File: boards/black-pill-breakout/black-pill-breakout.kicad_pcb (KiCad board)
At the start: 2 copper layers, 79 x 47 mm, 24 parts

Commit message: Layout idea #2
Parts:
- removed the REF** at (124.5, 78.7)
- removed the REF** at (144.8, 81.3)
- removed the REF** at (144.8, 83.8)
- removed the REF** at (182.9, 96.5)
- removed the REF** at (200.7, 87.6)
- removed the REF** at (124.5, 81.3)
- removed the REF** at (200.7, 90.2)
- removed the REF** at (144.8, 78.7)
- removed the REF** at (200.7, 85.1)
- removed the REF** at (124.5, 83.8)
- added REF**: PinSocket_1x06_P2.54mm_Vertical, Connector_PinSocket_2.54mm:PinSocket_1x06_P2.54mm_Vertical, F.Cu at (147.3, 83.8)
- added REF**: PinSocket_1x06_P2.54mm_Vertical, Connector_PinSocket_2.54mm:PinSocket_1x06_P2.54mm_Vertical, F.Cu at (167.6, 83.8)
- added REF**: PinSocket_1x06_P2.54mm_Vertical, Connector_PinSocket_2.54mm:PinSocket_1x06_P2.54mm_Vertical, F.Cu at (147.3, 81.3)
- added REF**: PinSocket_1x06_P2.54mm_Vertical, Connector_PinSocket_2.54mm:PinSocket_1x06_P2.54mm_Vertical, F.Cu at (167.6, 78.7)
- added REF**: PinSocket_1x06_P2.54mm_Vertical, Connector_PinSocket_2.54mm:PinSocket_1x06_P2.54mm_Vertical, F.Cu at (147.3, 78.7)
- added REF**: PinSocket_1x06_P2.54mm_Vertical, Connector_PinSocket_2.54mm:PinSocket_1x06_P2.54mm_Vertical, F.Cu at (167.6, 81.3)
- moved REF** 42.1 mm to (137.2, 81.3), turned to 270 degrees
- moved REF** 5.39 mm to (181.6, 97.8)
- moved REF** 4.43 mm to (148.6, 104.1)

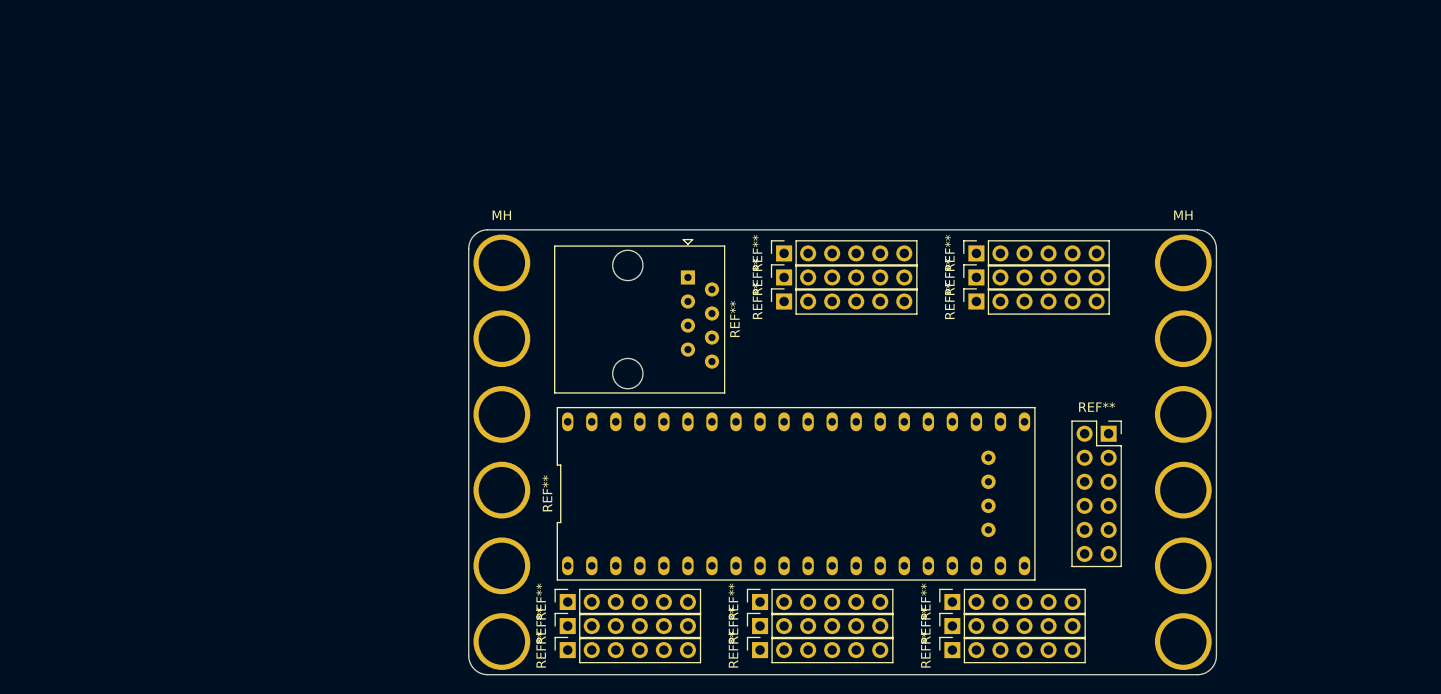
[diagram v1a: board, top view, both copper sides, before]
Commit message: Done routing, pre-silkscreen
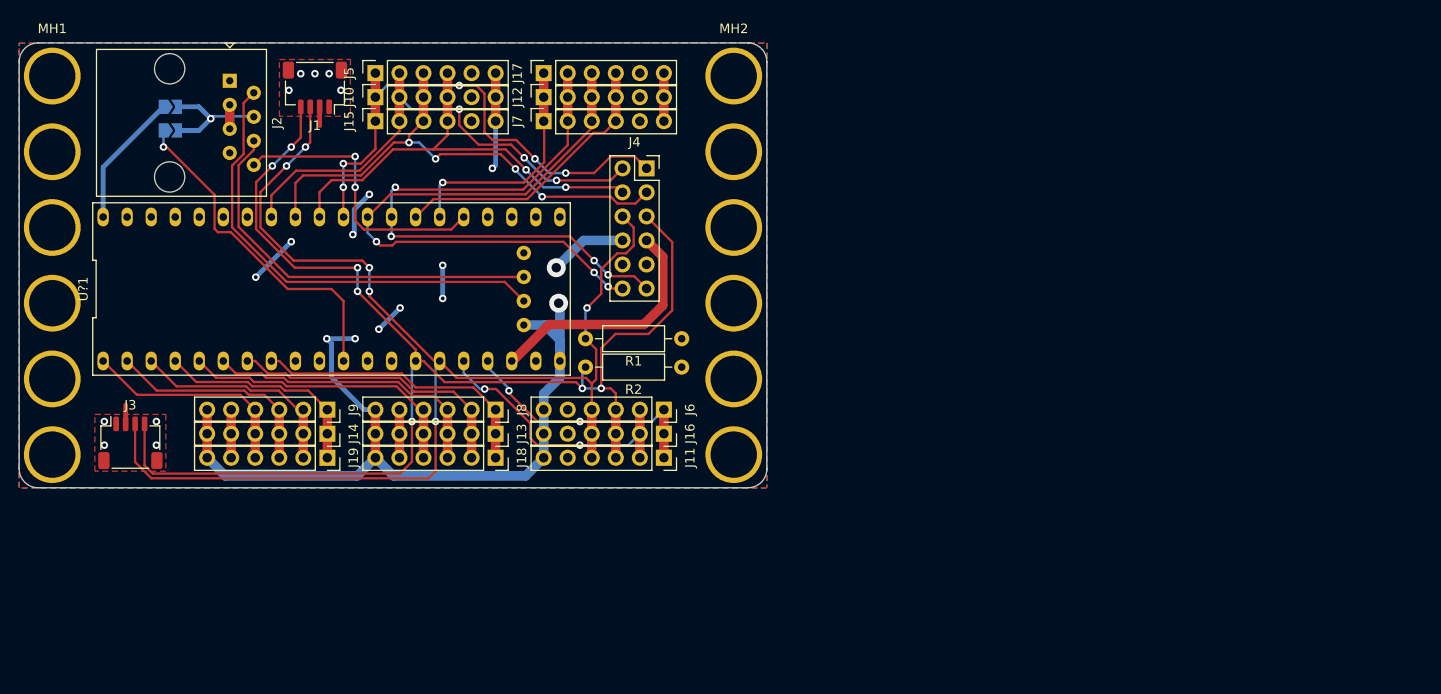
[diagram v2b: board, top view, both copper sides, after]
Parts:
- removed MH (x2): brick-1x6, brick-4_9id-6_0od:brick-1x6
- removed REF** (x15): PinSocket_1x06_P2.54mm_Vertical, Connector_PinSocket_2.54mm:PinSocket_1x06_P2.54mm_Vertical
- removed REF**: weact-blackpill, usb-c-pill:weact-blackpill
- removed REF**: RJ45_Amphenol_54602-x08_Horizontal, Connector_RJ:RJ45_Amphenol_54602-x08_Horizontal
- removed REF**: PinSocket_2x06_P2.54mm_Vertical, Connector_PinSocket_2.54mm:PinSocket_2x06_P2.54mm_Vertical
- added J1: Conn_01x04_MountingPin, Connector_JST:JST_SH_SM04B-SRSS-TB_1x04-1MP_P1.00mm_Horizontal, F.Cu at (97.8, 61.2)
- added J10: Conn_01x06, Connector_PinSocket_2.54mm:PinSocket_1x06_P2.54mm_Vertical, F.Cu at (104.1, 62.2)
- added J11: Conn_01x06, Connector_PinSocket_2.54mm:PinSocket_1x06_P2.54mm_Vertical, F.Cu at (134.6, 100.3)
- added J12: Conn_01x06, Connector_PinSocket_2.54mm:PinSocket_1x06_P2.54mm_Vertical, F.Cu at (121.9, 62.2)
- added J13: Conn_01x06, Connector_PinSocket_2.54mm:PinSocket_1x06_P2.54mm_Vertical, F.Cu at (116.8, 97.8)
- added J14: Conn_01x06, Connector_PinSocket_2.54mm:PinSocket_1x06_P2.54mm_Vertical, F.Cu at (99.1, 97.8)
- added J15: Conn_01x06, Connector_PinSocket_2.54mm:PinSocket_1x06_P2.54mm_Vertical, F.Cu at (104.1, 64.8)
- added J16: Conn_01x06, Connector_PinSocket_2.54mm:PinSocket_1x06_P2.54mm_Vertical, F.Cu at (134.6, 97.8)
- added J17: Conn_01x06, Connector_PinSocket_2.54mm:PinSocket_1x06_P2.54mm_Vertical, F.Cu at (121.9, 59.7)
- added J18: Conn_01x06, Connector_PinSocket_2.54mm:PinSocket_1x06_P2.54mm_Vertical, F.Cu at (116.8, 100.3)
- added J19: Conn_01x06, Connector_PinSocket_2.54mm:PinSocket_1x06_P2.54mm_Vertical, F.Cu at (99.1, 100.3)
- added J2: 8P8C, Connector_RJ:RJ45_Amphenol_54602-x08_Horizontal, F.Cu at (88.8, 60.5)
- added J3: Conn_01x04_MountingPin, Connector_JST:JST_SH_SM04B-SRSS-TB_1x04-1MP_P1.00mm_Horizontal, F.Cu at (78.2, 98.8)
- added J4: Conn_02x06_Counter_Clockwise, Connector_PinSocket_2.54mm:PinSocket_2x06_P2.54mm_Vertical, F.Cu at (132.8, 69.8)
- added J5: Conn_01x06, Connector_PinSocket_2.54mm:PinSocket_1x06_P2.54mm_Vertical, F.Cu at (104.1, 59.7)
- added J6: Conn_01x06, Connector_PinSocket_2.54mm:PinSocket_1x06_P2.54mm_Vertical, F.Cu at (134.6, 95.2)
- added J7: Conn_01x06, Connector_PinSocket_2.54mm:PinSocket_1x06_P2.54mm_Vertical, F.Cu at (121.9, 64.8)
- added J8: Conn_01x06, Connector_PinSocket_2.54mm:PinSocket_1x06_P2.54mm_Vertical, F.Cu at (116.8, 95.2)
- added J9: Conn_01x06, Connector_PinSocket_2.54mm:PinSocket_1x06_P2.54mm_Vertical, F.Cu at (99.1, 95.2)
- added JP1: SolderJumper_2_Open, Jumper:SolderJumper-2_P1.3mm_Open_TrianglePad1.0x1.5mm, B.Cu at (82.5, 63.2)
- added JP2: SolderJumper_2_Open, Jumper:SolderJumper-2_P1.3mm_Open_TrianglePad1.0x1.5mm, B.Cu at (82.5, 65.8)
- added MH1: Conn_01x06, brick-4_9id-6_0od:brick-1x6, F.Cu at (70.0, 60.0)
- added MH2: Conn_01x06, brick-4_9id-6_0od:brick-1x6, F.Cu at (142.0, 60.0)
- added R1: DNP, Resistor_THT:R_Axial_DIN0207_L6.3mm_D2.5mm_P10.16mm_Horizontal, F.Cu at (136.5, 87.8)
- added R2: DNP, Resistor_THT:R_Axial_DIN0207_L6.3mm_D2.5mm_P10.16mm_Horizontal, F.Cu at (136.5, 90.8)
- added U?1: weact-black-pill, usb-c-pill:weact-blackpill, F.Cu at (99.5, 82.5)
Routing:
- net /I2C-SCL: track 0.00 -> 140.7 mm, vias 0 -> 7
- net /I2C-SDA: track 0.00 -> 137.1 mm, vias 0 -> 6
- net +3V3: track 0.00 -> 130.4 mm, vias 0 -> 13
- net /USART-RX: track 0.00 -> 64.8 mm, vias 0 -> 3
- net /USART-TX: track 0.00 -> 62.5 mm, vias 0 -> 4
- net /~SPI-CS: track 0.00 -> 54.3 mm, vias 0 -> 5
- net /SPI-CIPO: track 0.00 -> 54.1 mm, vias 0 -> 4
- net /SPI-COPI: track 0.00 -> 53.5 mm, vias 0 -> 3
- net /SWDIO: track 0.00 -> 49.2 mm
- net /SPI-SCK: track 0.00 -> 47.4 mm, vias 0 -> 2
- net /SWCLK: track 0.00 -> 42.1 mm
- net +5V: track 0.00 -> 40.2 mm
- net /SWO: track 0.00 -> 35.9 mm, vias 0 -> 1
- net /GPIO6: track 0.00 -> 30.9 mm
- net /GPIO7: track 0.00 -> 30.9 mm
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- added copper zone on F.Cu, net +3V3
- added copper zone on B.Cu, net GND
- added copper zone on F.Cu, net GND

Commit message: Board Complete - Pre-Export
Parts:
- added J20: Conn_01x04, Connector_PinSocket_2.54mm:PinSocket_1x04_P2.54mm_Vertical, F.Cu at (76.2, 78.7)
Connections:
- U?1 pad 10: Net-(U?1-Pad10) -> /GPIO8
- U?1 pad 8: /GPIO8 -> Net-(U?1-Pad8)
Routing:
- net Net-(J20-Pad4): track 0.00 -> 19.2 mm, vias 0 -> 1
- net Net-(J20-Pad3): track 0.00 -> 15.6 mm, vias 0 -> 1
- net Net-(J20-Pad2): track 0.00 -> 12.5 mm
- net Net-(J20-Pad1): track 0.00 -> 9.64 mm
- net /GPIO8: track 30.9 -> 25.8 mm
- net +3V3: track 130.4 -> 129.2 mm
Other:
- board text added: "1"
- board text added: "1: GND"
- board text added: "2"
- board text added: "2: DIO"
- board text added: "3"
- board text added: "3: GND"
- board text added: "3v3"
- board text added: "4"
- board text added: "4: JMP"
- board text added: "5"
- board text added: "5: GND"
- board text added: "5v0"
- board text added: "6"
- board text added: "6: SCK"
- board text added: "7"
- board text added: "7: 3v3"
- board text added: "8"
- board text added: "8: ~RST"
- board text added: "@bitshiftmask"
- board text added: "Board Design Weekend - Ep. 000"
- board text added: "Brick Board Breakout"
- board text added: "CIPO"
- board text added: "COPI"
- board text added: "CSn"
- board text added: "CTS"
- board text added: "DEBUG"
- board text added: "GND"
- board text added: "GPIO1"
- board text added: "GPIO2"
- board text added: "GPIO3"
- board text added: "GPIO4"
- board text added: "GPIO5"
- board text added: "GPIO6"
- board text added: "GPIO7"
- board text added: "GPIO8"
- board text added: "GPIOs"
- board text added: "I2C"
- board text added: "INT"
- board text added: "JLCJLCJLCJLC"
- board text added: "JMP"
- board text added: "PA00"
- board text added: "PA01"
- board text added: "PA02"
- board text added: "PA03"
- board text added: "PA04"
- board text added: "PA05"
- board text added: "PA06"
- board text added: "PA07"
- board text added: "PA08"
- board text added: "PA09"
- board text added: "PA10"
- board text added: "PA15"
- board text added: "PB00"
- board text added: "PB01"
- board text added: "PB02"
- board text added: "PB06"
- board text added: "PB07"
- board text added: "PB08"
- board text added: "PB09"
- board text added: "PB10"
- board text added: "PB12"
- board text added: "PB13"
- board text added: "PB14"
- board text added: "PB15"
- board text added: "QWIIC"
- board text added: "RST"
- board text added: "RTS"
- board text added: "RXD"
- board text added: "SCK"
- board text added: "SCL"
- board text added: "SCLK"
- board text added: "SDA"
- board text added: "SPI"
- board text added: "SWO"
- board text added: "TXD"
- board text added: "UART"
- board text added: "WeAct USB-C Pill"
- board text added: "v0.1.0 - Feb. 2021"
- board text added: "~CS"
- board text added: "~INT"
- board text added: "~RST"

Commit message: Update
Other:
- board text added: "4: 5v0/SWO JMP"
- board text removed: "4: JMP"
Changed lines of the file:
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@@
   (page A4)
   (layers
-    (0 F.Cu signal hide)
-    (31 B.Cu signal hide)
+    (0 F.Cu signal)
+    (31 B.Cu signal)
     (32 B.Adhes user)
     (33 F.Adhes user)
@@
       (layerselection 0x010fc_ffffffff)
       (usegerberextensions false)
-      (usegerberattributes true)
+      (usegerberattributes false)
       (usegerberadvancedattributes true)
       (creategerberjobfile true)
@@
       (outputformat 1)
       (mirror false)
-      (drillshape 1)
+      (drillshape 0)
       (scaleselection 1)
-      (outputdirectory ""))
+      (outputdirectory "gerbers/"))
   )
   (net 0 "")
@@
       (effects (font (size 1 1) (thickness 0.15)))
     )
-    (fp_text user %R (at 0 3.81 90) (layer F.Fab)
-      (effects (font (size 1 1) (thickness 0.15)))
-    )
     (fp_line (start -1.27 -1.27) (end 0.635 -1.27) (layer F.Fab) (width 0.1))
     (fp_line (start 0.635 -1.27) (end 1.27 -0.635) (layer F.Fab) (width 0.1))
@@
     (fp_line (start 1.75 9.4) (end -1.8 9.4) (layer F.CrtYd) (width 0.05))
     (fp_line (start -1.8 9.4) (end -1.8 -1.8) (layer F.CrtYd) (width 0.05))
+    (fp_text user %R (at 0 3.81 90) (layer F.Fab)
+      (effects (font (size 1 1) (thickness 0.15)))
+    )
     (pad 4 thru_hole oval (at 0 7.62) (size 1.7 1.7) (drill 1) (layers *.Cu *.Mask)
       (net 36 "Net-(J20-Pad4)"))
@@
       (effects (font (size 1 1) (thickness 0.15)))
     )
-    (pad MP smd roundrect (at 2.8 1.875) (size 1.2 1.8) (layers F.Cu F.Paste F.Mask) (roundrect_rratio 0.208333)
-      (net 1 GND))
-    (pad MP smd roundrect (at -2.8 1.875) (size 1.2 1.8) (layers F.Cu F.Paste F.Mask) (roundrect_rratio 0.208333)
+    (pad MP smd roundrect (at 2.8 1.875) (size 1.2 1.8) (layers F.Cu F.Paste F.Mask) (roundrect_rratio 0.2083325)
+      (net 1 GND))
+    (pad MP smd roundrect (at -2.8 1.875) (size 1.2 1.8) (layers F.Cu F.Paste F.Mask) (roundrect_rratio 0.2083325)
       (net 1 GND))
     (pad 4 smd roundrect (at 1.5 -2) (size 0.6 1.55) (layers F.Cu F.Paste F.Mask) (roundrect_rratio 0.25)
@@
       (effects (font (size 1 1) (thickness 0.15)))
     )
-    (pad MP smd roundrect (at 2.8 1.875 180) (size 1.2 1.8) (layers F.Cu F.Paste F.Mask) (roundrect_rratio 0.208333)
-      (net 1 GND))
-    (pad MP smd roundrect (at -2.8 1.875 180) (size 1.2 1.8) (layers F.Cu F.Paste F.Mask) (roundrect_rratio 0.208333)
+    (pad MP smd roundrect (at 2.8 1.875 180) (size 1.2 1.8) (layers F.Cu F.Paste F.Mask) (roundrect_rratio 0.2083325)
+      (net 1 GND))
+    (pad MP smd roundrect (at -2.8 1.875 180) (size 1.2 1.8) (layers F.Cu F.Paste F.Mask) (roundrect_rratio 0.2083325)
       (net 1 GND))
     (pad 4 smd roundrect (at 1.5 -2 180) (size 0.6 1.55) (layers F.Cu F.Paste F.Mask) (roundrect_rratio 0.25)
@@
     (effects (font (size 1 1) (thickness 0.15)) (justify left))
   )
-  (gr_text "4: JMP" (at 74.75 64) (layer F.SilkS)
+  (gr_text "4: 5v0/SWO JMP" (at 74.75 64) (layer F.SilkS)
     (effects (font (size 1 1) (thickness 0.15)) (justify left))
   )
